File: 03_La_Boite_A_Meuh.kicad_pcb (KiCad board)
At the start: 2 copper layers, 100 x 100 mm, 65 parts, among them J1 Conn_01x02, J10 Conn_01x01, J11 Conn_01x04, J12 Conn_01x01, J13 Conn_01x01, J14 Conn_01x01, J15 Conn_01x01, J16 Conn_01x01, J17 Conn_01x01, J18 Conn_01x02, J19 Conn_01x01, J2 Conn_01x02, J20 Conn_01x01, J21 Conn_01x01, J22 Conn_01x01, J23 Conn_01x01, J24 Conn_01x01, J25 Conn_01x01, J26 Conn_01x02, J27 Conn_01x02, J28 Conn_01x03, J29 Conn_01x02, J3 Conn_01x02, J4 Conn_01x02, J5 Conn_01x02, J6 Conn_01x04, J7 Conn_01x04, J8 Conn_01x04, J9 Conn_01x01, Q1 2N7002, U1 DFR0299, U2 ESP32-DEVKITC, U3 PAM8302AAS, U4 Batt_Alim

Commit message: maj
simplification dfr
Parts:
- removed BT1: Battery_Cell, Battery:BatteryHolder_Keystone_1042_1x18650
- removed J16, J17, J19, J20, J21, J22, J23, J24: Conn_01x01, Connector_PinHeader_2.54mm:PinHeader_1x01_P2.54mm_Vertical
- removed J28: Conn_01x03, Connector_JST:JST_XH_S3B-XH-A_1x03_P2.50mm_Horizontal
- removed REF**: KiCad-Logo2_5mm_SilkScreen, Symbol:KiCad-Logo2_5mm_SilkScreen
- removed REF**: OSHW-Logo2_7.3x6mm_SilkScreen, Symbol:OSHW-Logo2_7.3x6mm_SilkScreen
- removed U1: DFR0299, Chimere:MODULE_DFR0299
- added C7: 100nF, Capacitor_SMD:C_0603_1608Metric, F.Cu at (176.0, 67.0)
- added R19: 10k, Resistor_SMD:R_0603_1608Metric_Pad1.05x0.95mm_HandSolder, F.Cu at (167.4, 71.5)
- added R22: 0, Resistor_SMD:R_0603_1608Metric_Pad1.05x0.95mm_HandSolder, F.Cu at (155.8, 95.9)
- added R23: 0, Resistor_SMD:R_0603_1608Metric_Pad1.05x0.95mm_HandSolder, F.Cu at (150.6, 70.5)
- added R24: 0, Resistor_SMD:R_0603_1608Metric_Pad1.05x0.95mm_HandSolder, F.Cu at (127.8, 100.8)
- added R25: 0, Resistor_SMD:R_0603_1608Metric_Pad1.05x0.95mm_HandSolder, F.Cu at (145.6, 70.5)
- added R26: 0, Resistor_SMD:R_0603_1608Metric_Pad1.05x0.95mm_HandSolder, F.Cu at (143.0, 70.5)
- added R27: 0, Resistor_SMD:R_0603_1608Metric_Pad1.05x0.95mm_HandSolder, F.Cu at (140.5, 70.5)
- added R29: 0, Resistor_SMD:R_0603_1608Metric_Pad1.05x0.95mm_HandSolder, F.Cu at (137.9, 70.5)
- added R31: 0, Resistor_SMD:R_0603_1608Metric_Pad1.05x0.95mm_HandSolder, F.Cu at (135.5, 70.5)
- added R32: 0, Resistor_SMD:R_0603_1608Metric_Pad1.05x0.95mm_HandSolder, F.Cu at (130.4, 95.9)
- added R33: 0, Resistor_SMD:R_0603_1608Metric_Pad1.05x0.95mm_HandSolder, F.Cu at (132.9, 70.5)
- added R35: 0, Resistor_SMD:R_0603_1608Metric_Pad1.05x0.95mm_HandSolder, F.Cu at (130.4, 70.5)
- added R37: 0, Resistor_SMD:R_0603_1608Metric_Pad1.05x0.95mm_HandSolder, F.Cu at (127.9, 70.5)
- added R38: 0, Resistor_SMD:R_0603_1608Metric_Pad1.05x0.95mm_HandSolder, F.Cu at (140.6, 95.8)
- added R40: 0, Resistor_SMD:R_0603_1608Metric_Pad1.05x0.95mm_HandSolder, F.Cu at (122.7, 70.5)
- added R42: 0, Resistor_SMD:R_0603_1608Metric_Pad1.05x0.95mm_HandSolder, F.Cu at (120.3, 89.1)
- added R43: 0, Resistor_SMD:R_0603_1608Metric_Pad1.05x0.95mm_HandSolder, F.Cu at (185.1, 84.6)
- added R44: 0, Resistor_SMD:R_0603_1608Metric_Pad1.05x0.95mm_HandSolder, F.Cu at (186.8, 93.6)
- added R45: 0, Resistor_SMD:R_0603_1608Metric_Pad1.05x0.95mm_HandSolder, F.Cu at (176.3, 91.1)
- added R46: 10k, Resistor_SMD:R_0603_1608Metric_Pad1.05x0.95mm_HandSolder, F.Cu at (176.3, 88.6)
- added R47: 0, Resistor_SMD:R_0603_1608Metric_Pad1.05x0.95mm_HandSolder, F.Cu at (186.8, 91.1)
- added R48: 0, Resistor_SMD:R_0603_1608Metric_Pad1.05x0.95mm_HandSolder, F.Cu at (176.3, 93.6)
- J1: value Conn_01x02 -> Micro_SD_Card; footprint Connector_JST:JST_XH_B2B-XH-A_1x02_P2.50mm_Vertical -> Connector_Card:microSD_HC_Molex_104031-0811
- J2: value Conn_01x02 -> Conn_01x06; footprint Connector_JST:JST_XH_B2B-XH-A_1x02_P2.50mm_Vertical -> Connector_PinSocket_2.54mm:PinSocket_1x06_P2.54mm_Vertical
- J3: value Conn_01x02 -> Conn_01x09; footprint Connector_JST:JST_XH_B2B-XH-A_1x02_P2.50mm_Vertical -> Connector_PinSocket_2.54mm:PinSocket_1x09_P2.54mm_Vertical
- J5: value Conn_01x02 -> Conn_02x02_Counter_Clockwise; footprint Connector_JST:JST_XH_B2B-XH-A_1x02_P2.50mm_Vertical -> Connector_PinSocket_2.54mm:PinSocket_2x02_P2.54mm_Vertical
- J9: value Conn_01x01 -> Conn_01x02; footprint Connector_PinHeader_2.54mm:PinHeader_1x01_P2.54mm_Vertical -> Connector_JST:JST_XH_B2B-XH-A_1x02_P2.50mm_Vertical
- R10: value 0 -> 1k
- R11: value 0 -> 10k
- R3: value 0 -> 100k
- U2: moved to F.Cu
- moved J7 75.1 mm to (154.5, 141.3), turned to 180 degrees
- moved J4 69.4 mm to (122.2, 113.1), turned to 270 degrees
- moved J2 65.3 mm to (186.9, 69.0)
- moved J11 61.5 mm to (154.5, 134.2), turned to 180 degrees
- moved J9 53.4 mm to (129.6, 113.1), turned to 270 degrees
- moved J8 48.2 mm to (154.5, 127.0), turned to 180 degrees
- moved R9 48.1 mm to (153.0, 120.7)
- moved J5 48.1 mm to (182.8, 93.6), turned to 270 degrees
- moved J1 48.0 mm to (175.6, 75.7)
- moved J12 47.9 mm to (133.0, 101.4)
- moved J13 45.1 mm to (135.4, 96.1)
- moved R8 42.5 mm to (147.2, 120.7), turned to 180 degrees
- moved J15 42.3 mm to (138.0, 100.2)
- moved R10 39.6 mm to (160.0, 113.5), turned to 90 degrees
- moved J27 38.2 mm to (114.7, 113.1)
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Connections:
- C4 pad 2: DFR_L -> DAC_Lout
- C5 pad 2: DFR_R -> DAC_Rout
- C6 pad 2: ESP_audio_out -> ESP_audio_out_div
- J1 pad 1: GND -> Net-(J1-Pad1)
- J1 pad 2: seg5 -> SD_CS
- J11 pad 2: 5V -> 3V3
- J2 pad 1: GND -> 3V3
- J2 pad 2: seg1 -> GND
- J3 pad 1: GND -> 5V
- J3 pad 2: next -> Net-(J3-Pad2)
- J4 pad 1: Net-(J4-Pad1) -> GND
- J5 pad 1: GND -> Net-(J5-Pad1)
- J5 pad 2: prev -> Net-(J5-Pad2)
- J7 pad 2: 5V -> 3V3
- J8 pad 2: 5V -> 3V3
- R10 pad 1: Net-(R10-Pad1) -> GND
- R10 pad 2: ESP2DFR -> ESP_audio_out_div
- R11 pad 1: Net-(R11-Pad1) -> SD_CS
- R11 pad 2: DFR2ESP -> 3V3
- R13 pad 1: 5V -> 3V3
- R14 pad 1: Net-(R14-Pad1) -> back0_div
- R15 pad 2: Net-(R14-Pad1) -> back0_div
- R3 pad 1: 3V3 -> ESP_audio_out_div
- R3 pad 2: Net-(R3-Pad2) -> ESP_audio_out
- U2 pad 23: Net-(R14-Pad1) -> Net-(R42-Pad2)
- U2 pad 28: LED_out -> Net-(J12-Pad1)
- U2 pad 29: bouton1 -> Net-(J13-Pad1)
- U2 pad 30: V_2_uC -> Net-(J15-Pad1)
- U2 pad 31: uC_2_V -> Net-(R38-Pad2)
- U2 pad 34: Net-(R11-Pad1) -> Net-(U2-Pad34)
- U2 pad 35: Net-(R10-Pad1) -> Net-(U2-Pad35)
- U2 pad 37: Net-(J9-Pad1) -> Net-(R22-Pad2)
- U2 pad 4: Net-(J12-Pad1) -> Net-(R23-Pad1)
- U2 pad 5: ESP_audio_out -> Net-(J14-Pad1)
- U2 pad 6: Net-(J13-Pad1) -> Net-(R25-Pad1)
- U2 pad 7: Net-(J14-Pad1) -> Net-(R26-Pad1)
- U2 pad 8: Net-(J15-Pad1) -> Net-(R27-Pad1)
- U4 pad 3: Net-(BT1-Pad1) -> Net-(J9-Pad1)
- U4 pad 4: Net-(BT1-Pad2) -> 5V
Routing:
- net GND: track 1137.1 -> 566.1 mm, vias 150 -> 13
- net SD_CS: track 0.00 -> 100.5 mm
- net 5V: track 121.7 -> 206.6 mm
- net out_BCLK: track 0.00 -> 73.7 mm
- net out_DIN: track 0.00 -> 73.6 mm, vias 0 -> 2
- net out_WSEL: track 0.00 -> 73.4 mm, vias 0 -> 2
- net SD_MOSI: track 0.00 -> 72.3 mm, vias 0 -> 2
- net ESP2DFR: track 71.1 -> 0.00 mm
- net DFR2ESP: track 70.9 -> 0.00 mm
- net Net-(BT1-Pad2): track 70.7 -> 0.00 mm
- net mic_BCLK: track 0.00 -> 62.9 mm
- net SD_MISO: track 0.00 -> 61.0 mm, vias 0 -> 2
- net mic_LRCL: track 0.00 -> 54.2 mm, vias 0 -> 1
- net SD_CLK: track 0.00 -> 51.6 mm, vias 0 -> 2
- net mic_DOUT: track 0.00 -> 49.4 mm, vias 0 -> 1
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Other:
- outline, holes or cut-outs redrawn
- board text added: "BAT"
- board text added: "Bouton"
- board text added: "La boite à Meuh 2021 03 02"
- board text added: "MIC"
- board text added: "Vext"
- board text removed: "Bouton1"
- board text removed: "La boite à Meuh 2020 12 23"
- board text removed: "SPK DFR"
- board text removed: "V_ext"
- board text removed: "next"
- board text removed: "prev"
- board text removed: "seg1"
- board text removed: "seg5"

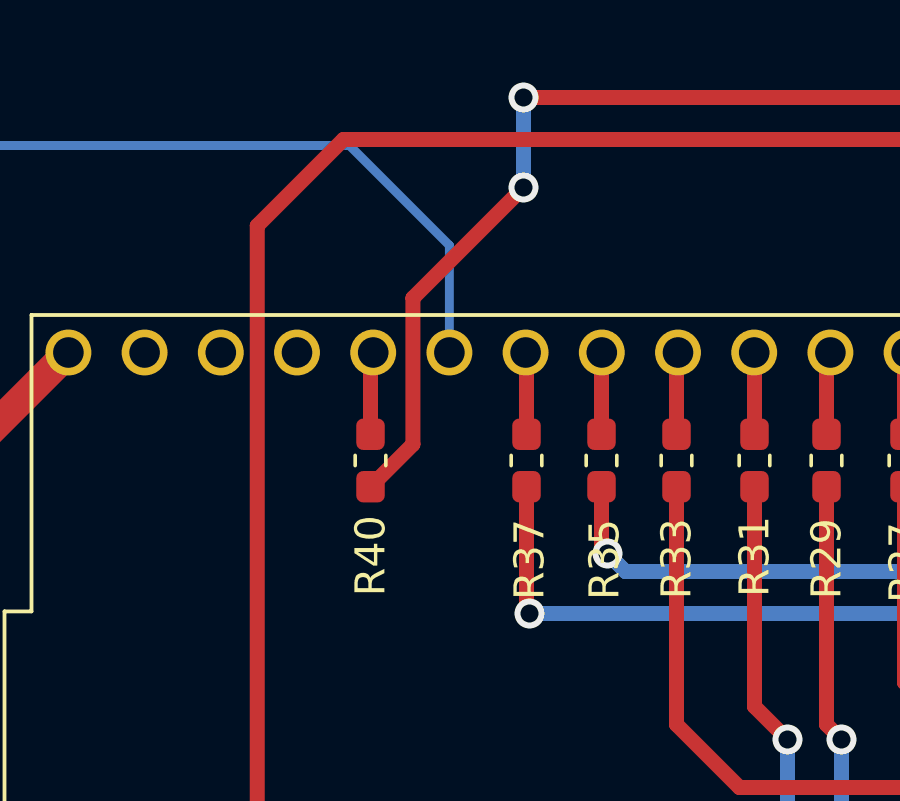
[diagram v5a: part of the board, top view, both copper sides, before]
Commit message: inversion miso et mosi sdcard
problème de pull-up au démarrage qui bloque l'esp32. Résolu en permutant les deux fils. schéma et routage corrigés
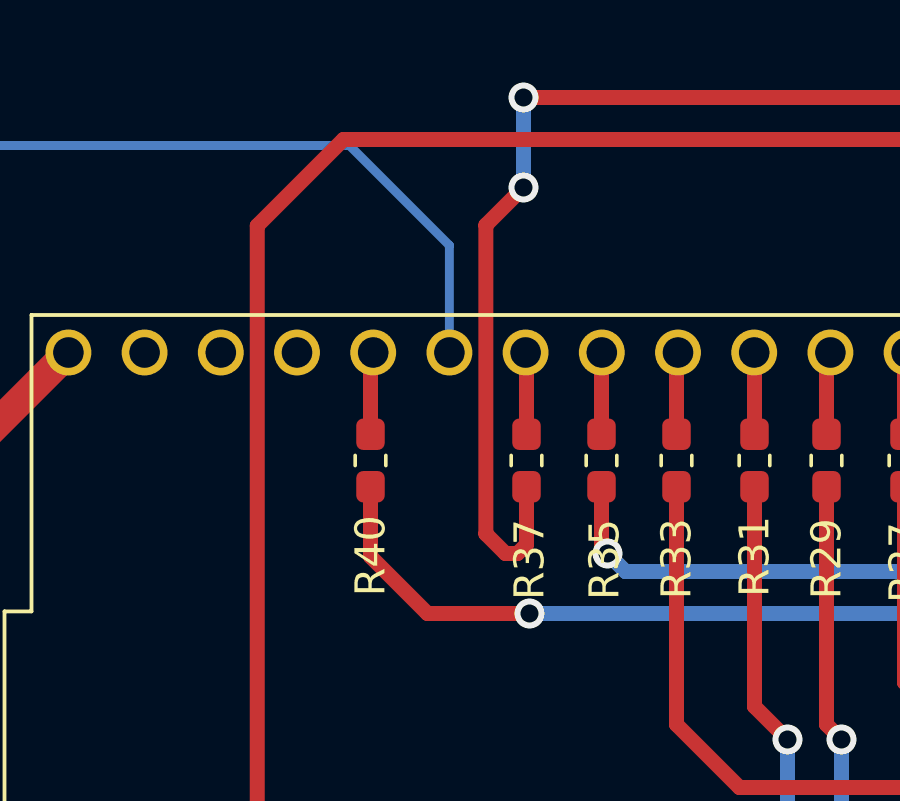
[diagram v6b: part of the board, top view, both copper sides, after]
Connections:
- R37 pad 2: SD_MISO -> SD_MOSI
- R40 pad 2: SD_MOSI -> SD_MISO
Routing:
- net SD_MISO: track 61.0 -> 65.3 mm
- net SD_MOSI: track 72.3 -> 75.9 mm

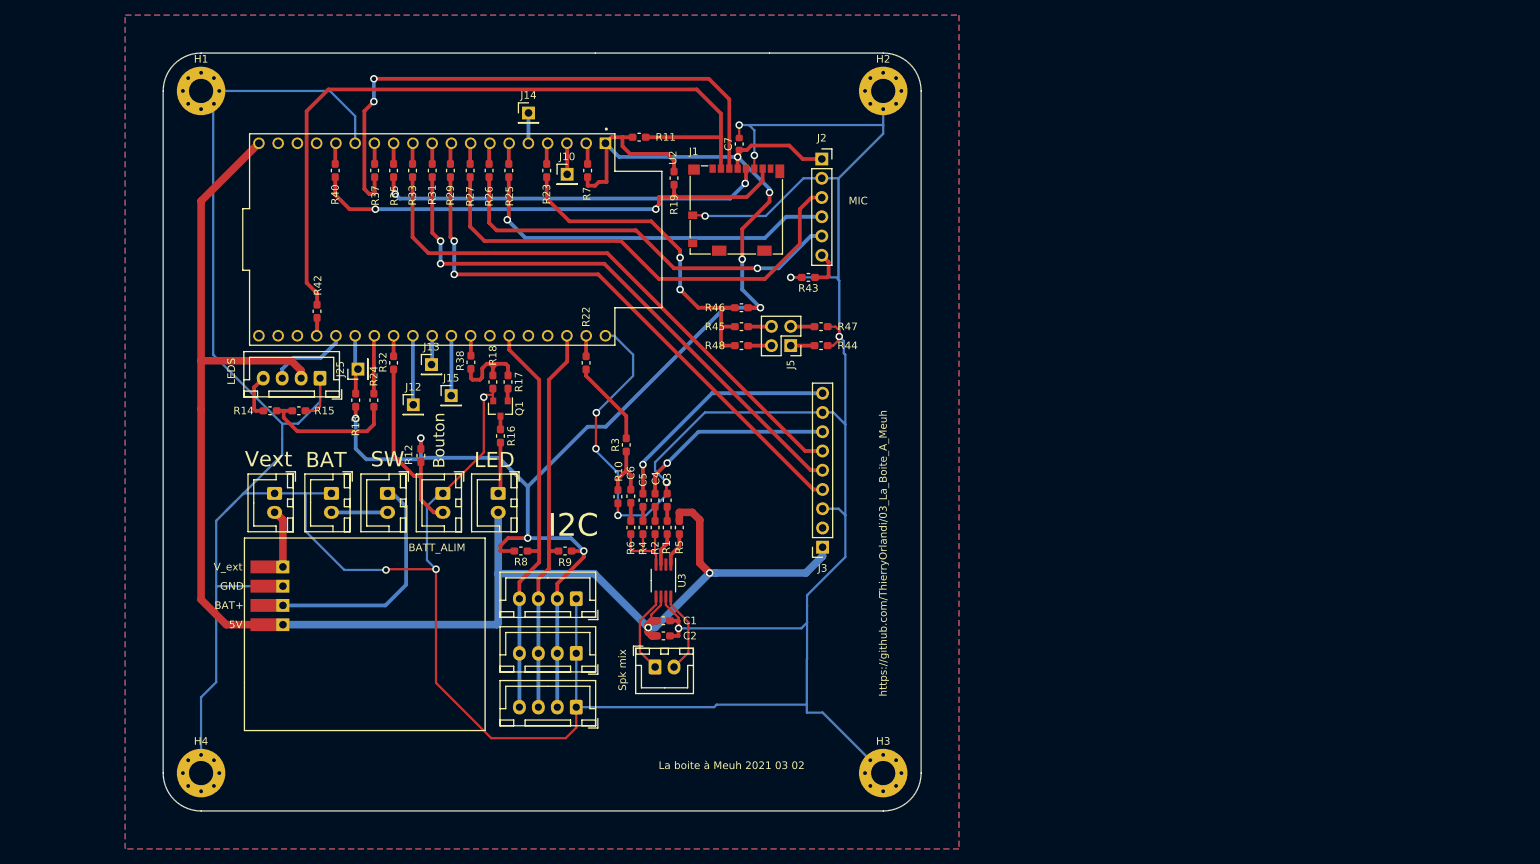
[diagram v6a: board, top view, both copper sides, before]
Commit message: ajout spi + placement + routage
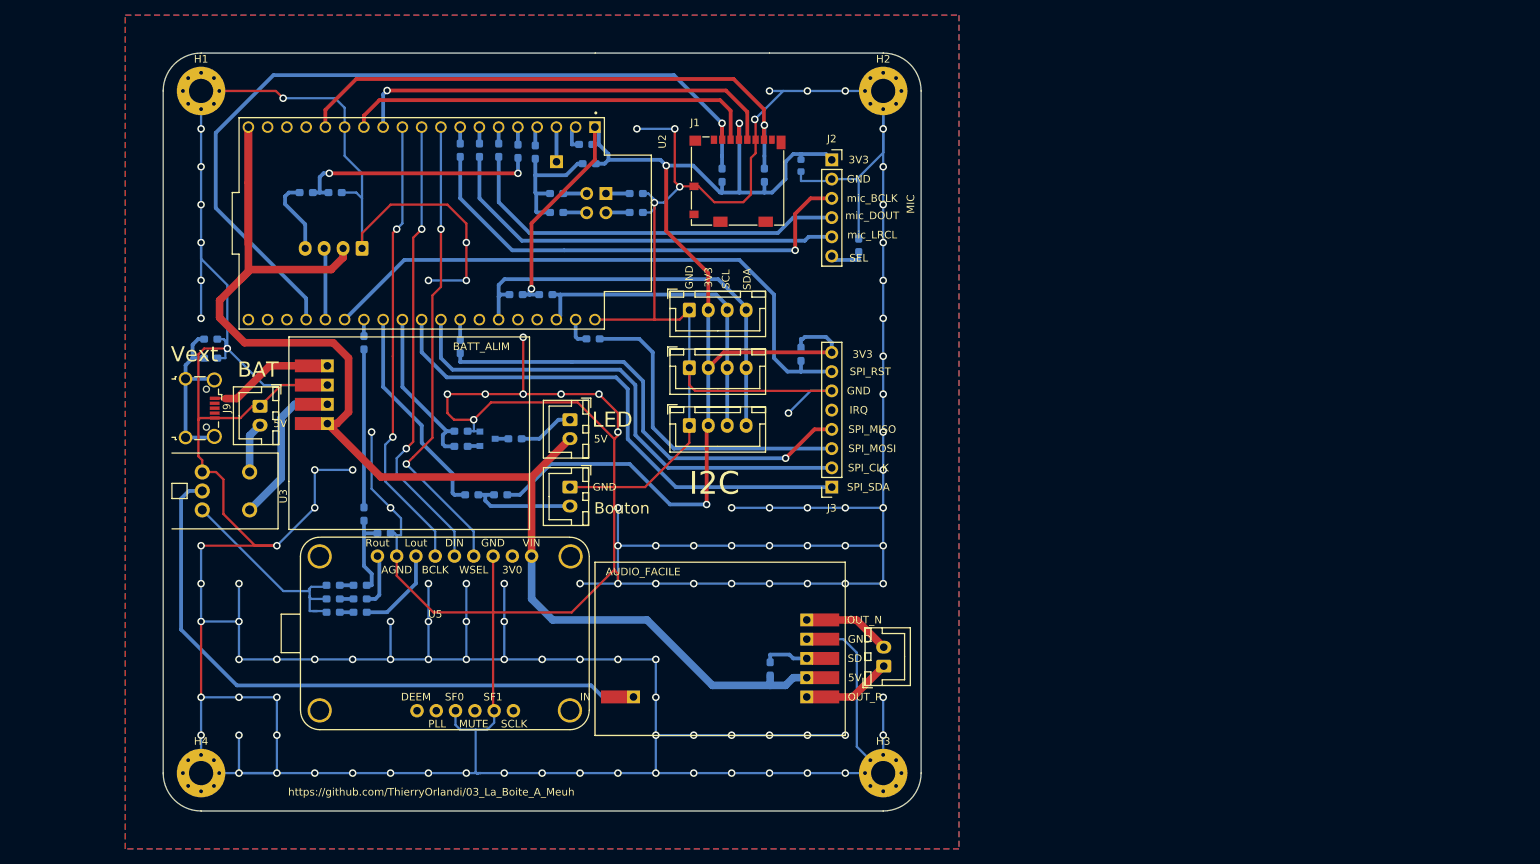
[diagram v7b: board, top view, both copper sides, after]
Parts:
- removed C2, C3: 100nF, Capacitor_SMD:C_0603_1608Metric_Pad1.05x0.95mm_HandSolder
- removed J12, J13, J14, J15, J25: Conn_01x01, Connector_PinHeader_2.54mm:PinHeader_1x01_P2.54mm_Vertical
- removed J27: Conn_01x02, Connector_JST:JST_XH_B2B-XH-A_1x02_P2.50mm_Vertical
- removed R29, R31, R33, R35, R37, R40, R42: 0, Resistor_SMD:R_0603_1608Metric_Pad1.05x0.95mm_HandSolder
- added R20: 0, Resistor_SMD:R_0603_1608Metric_Pad1.05x0.95mm_HandSolder, B.Cu at (146.8, 68.0)
- added U1: Audio_Facile, Chimere:Audio_Facile, F.Cu at (184.9, 140.0)
- added U5: UDA1334_ADAFRUIT, Chimere:Adafruit_UDA1334, F.Cu at (137.2, 131.6)
- C1: value 1uF -> 100nF; moved to B.Cu
- C4, C5, C6, C7, J10, J5, J6, Q1, R1, R10, R11, R12, R13, R14, R15, R16, R17, R18, R19, R22, R23, R24, R25, R26, R27, R3, R32, R38, R43, R44, R45, R46, R47, R48, R5, R7, R8, R9: moved to B.Cu
- J3: value Conn_01x09 -> Conn_01x08; footprint Connector_PinSocket_2.54mm:PinSocket_1x09_P2.54mm_Vertical -> Connector_PinSocket_2.54mm:PinSocket_1x08_P2.54mm_Vertical
- J9: value Conn_01x02 -> USB_B_Micro; footprint Connector_JST:JST_XH_B2B-XH-A_1x02_P2.50mm_Vertical -> Connector_USB:USB_Micro-B_Wuerth_629105150521_CircularHoles
- R2, R4, R6: value 100k -> 1k; moved to B.Cu
- U3: value PAM8302AAS -> rot_pot_rot_sw; footprint Package_SO:MSOP-8_3x3mm_P0.65mm -> Chimere:PTR901
- moved C1 69.0 mm to (106.3, 95.3), turned to 0 degrees
- moved R1 65.2 mm to (106.3, 92.7), turned to 0 degrees
- moved U3 62.0 mm to (105.2, 112.8), turned to 180 degrees
- moved R13 59.1 mm to (184.2, 94.7), turned to 270 degrees
- moved J7 54.5 mm to (169.4, 88.9), turned to 0 degrees
- moved R2 43.9 mm to (122.4, 128.8), turned to 0 degrees
- moved R4 41.9 mm to (122.4, 127.0), turned to 0 degrees
- moved C4 41.6 mm to (126.0, 128.8), turned to 0 degrees
- moved J11 40.5 mm to (169.4, 96.5), turned to 0 degrees
- moved R6 40.0 mm to (122.4, 125.2), turned to 0 degrees
- moved C5 39.5 mm to (126.0, 127.0), turned to 0 degrees
- moved C6 37.6 mm to (126.0, 125.2), turned to 0 degrees
- moved R3 35.8 mm to (126.5, 115.8)
- moved R9 33.9 mm to (150.5, 86.9), turned to 180 degrees
- moved R8 33.8 mm to (146.6, 86.9), turned to 0 degrees
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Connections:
- C1 pad 1: GND -> Net-(C1-Pad1)
- C1 pad 2: 5V -> GND
- J3 pad 1: 5V -> SPI_SDA
- J3 pad 2: Net-(J3-Pad2) -> SPI_SCK
- J3 pad 3: GND -> SPI_MOSI
- J3 pad 4: out_WSEL -> SPI_MISO
- J3 pad 5: out_DIN -> Net-(J3-Pad5)
- J3 pad 6: out_BCLK -> GND
- J3 pad 7: DAC_Lout -> SPI_RST
- J3 pad 8: GND -> 3V3
- J4 pad 2: Net-(J4-Pad2) -> VBAT1
- J9 pad 1: Net-(J9-Pad1) -> /Batt_alim/V_ext
- J9 pad 2: Net-(J4-Pad2) -> Net-(J9-Pad2)
- R1 pad 1: Net-(R1-Pad1) -> Net-(C1-Pad1)
- R1 pad 2: Net-(C3-Pad1) -> GND
- R13 pad 2: Net-(J25-Pad1) -> SPI_RST
- R22 pad 1: ESP_audio_out -> SPI_MOSI
- R24 pad 1: back0_div -> ESP_audio_out
- R38 pad 1: LED_out -> SPI_MISO
- U2 pad 10: Net-(R31-Pad1) -> out_DIN
- U2 pad 11: Net-(R33-Pad1) -> out_BCLK
- U2 pad 12: Net-(R35-Pad1) -> SD_CLK
- U2 pad 13: Net-(R37-Pad1) -> SD_MOSI
- U2 pad 15: Net-(R40-Pad1) -> SD_MISO
- U2 pad 23: Net-(R42-Pad2) -> SD_CS
- U2 pad 25: Net-(J25-Pad1) -> SPI_RST
- U2 pad 28: Net-(J12-Pad1) -> LED_out
- U2 pad 29: Net-(J13-Pad1) -> SPI_SDA
- U2 pad 30: Net-(J15-Pad1) -> SPI_SCK
- U2 pad 9: Net-(R29-Pad1) -> out_WSEL
- U3 pad 1: Net-(R5-Pad2) -> VBAT2
- U3 pad 2: Net-(U3-Pad2) -> VBAT1
- U3 pad 3: Net-(R1-Pad1) -> GND
- U3 pad 4: Net-(R2-Pad1) -> Net-(U1-Pad6)
- U3 pad 5: Net-(J29-Pad1) -> Net-(R2-Pad1)
- U4 pad 3: Net-(J9-Pad1) -> VBAT2
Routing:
- net GND: track 566.1 -> 1086.9 mm, vias 13 -> 123
- net Net-(U1-Pad6): track 0.00 -> 86.4 mm
- net SPI_RST: track 0.00 -> 80.0 mm
- net SPI_SDA: track 0.00 -> 69.7 mm
- net SPI_SCK: track 0.00 -> 66.5 mm
- net SPI_MISO: track 0.00 -> 60.9 mm, vias 0 -> 1
- net SPI_MOSI: track 0.00 -> 42.4 mm
- net Net-(J9-Pad1): track 33.4 -> 0.00 mm
- net TILT: track 45.4 -> 17.6 mm, vias 2 -> 0
- net Net-(R32-Pad2): track 2.70 -> 28.4 mm
- net DAC_Rout: track 31.7 -> 7.11 mm, vias 1 -> 0
- net Net-(C1-Pad1): track 0.00 -> 23.7 mm
- net VBAT2: track 0.00 -> 23.2 mm
- net SD_MOSI: track 75.9 -> 55.1 mm, vias 2 -> 0
- net 5V: track 206.6 -> 188.8 mm, vias 2 -> 0
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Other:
- board text added: "3V3"
- board text added: "5V"
- board text added: "GND"
- board text added: "IRQ"
- board text added: "S0"
- board text added: "SCL"
- board text added: "SDA"
- board text added: "SEL"
- board text added: "SPI_CLK"
- board text added: "SPI_MISO"
- board text added: "SPI_MOSI"
- board text added: "SPI_RST"
- board text added: "SPI_SDA"
- board text added: "TILT"
- board text added: "backS0"
- board text added: "mic_BCLK"
- board text added: "mic_DOUT"
- board text added: "mic_LRCL"
- board text removed: "La boite à Meuh 2021 03 02"
- board text removed: "SW"
- board text removed: "Spk mix"

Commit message: correction pcb
ajout infos sur silk
changement connecteur jst xh 4 points pour un coudé.
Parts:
- J6: footprint Connector_JST:JST_XH_B4B-XH-A_1x04_P2.50mm_Vertical -> Connector_JST:JST_XH_S4B-XH-A_1x04_P2.50mm_Horizontal
- moved J6 6.35 mm to (121.5, 85.0), turned to 90 degrees
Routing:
- net 5V: track 188.8 -> 183.3 mm
- net GND: track 1086.9 -> 1090.8 mm, vias 123 -> 124
- net S0: track 9.47 -> 12.3 mm
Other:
- board text added: "La Boite a Meuh 2021 04 07"
- board text added: "USB Vext"
- board text removed: "Vext"
